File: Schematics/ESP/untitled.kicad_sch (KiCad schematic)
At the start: 10 parts, among them J10 Conn_01x03_Socket, J11 Conn_01x02_Pin, J12 Conn_01x02_Pin, J14 Conn_02x19_Odd_Even, J16 Conn_02x19_Odd_Even, J2 Conn_01x06_Pin, J7 Conn_01x07_Pin, J9 Conn_01x03_Socket

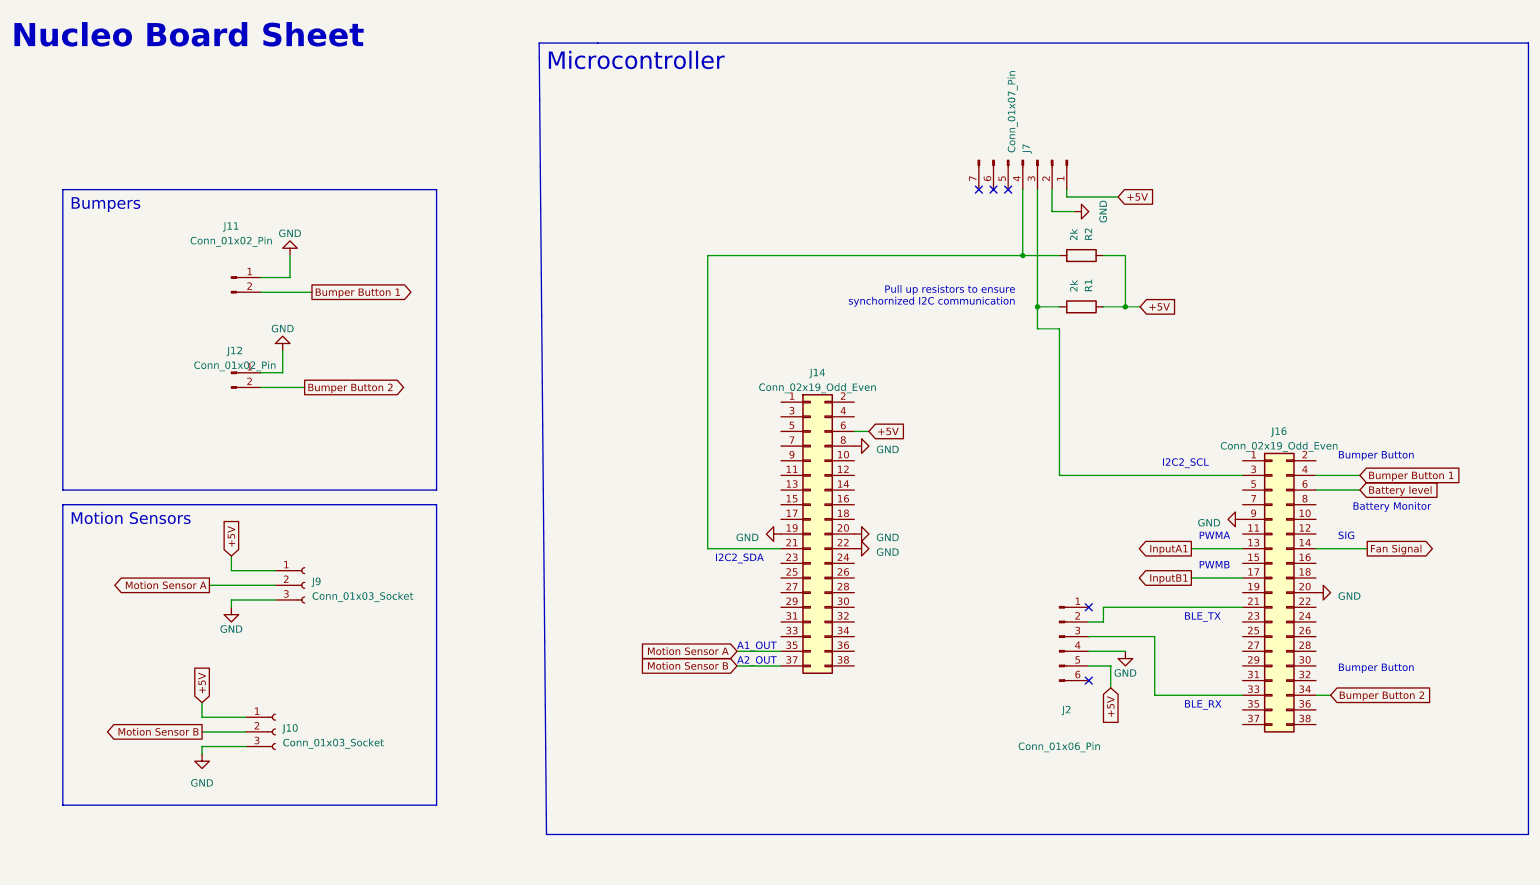
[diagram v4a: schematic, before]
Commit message: PCB layout done no wiring
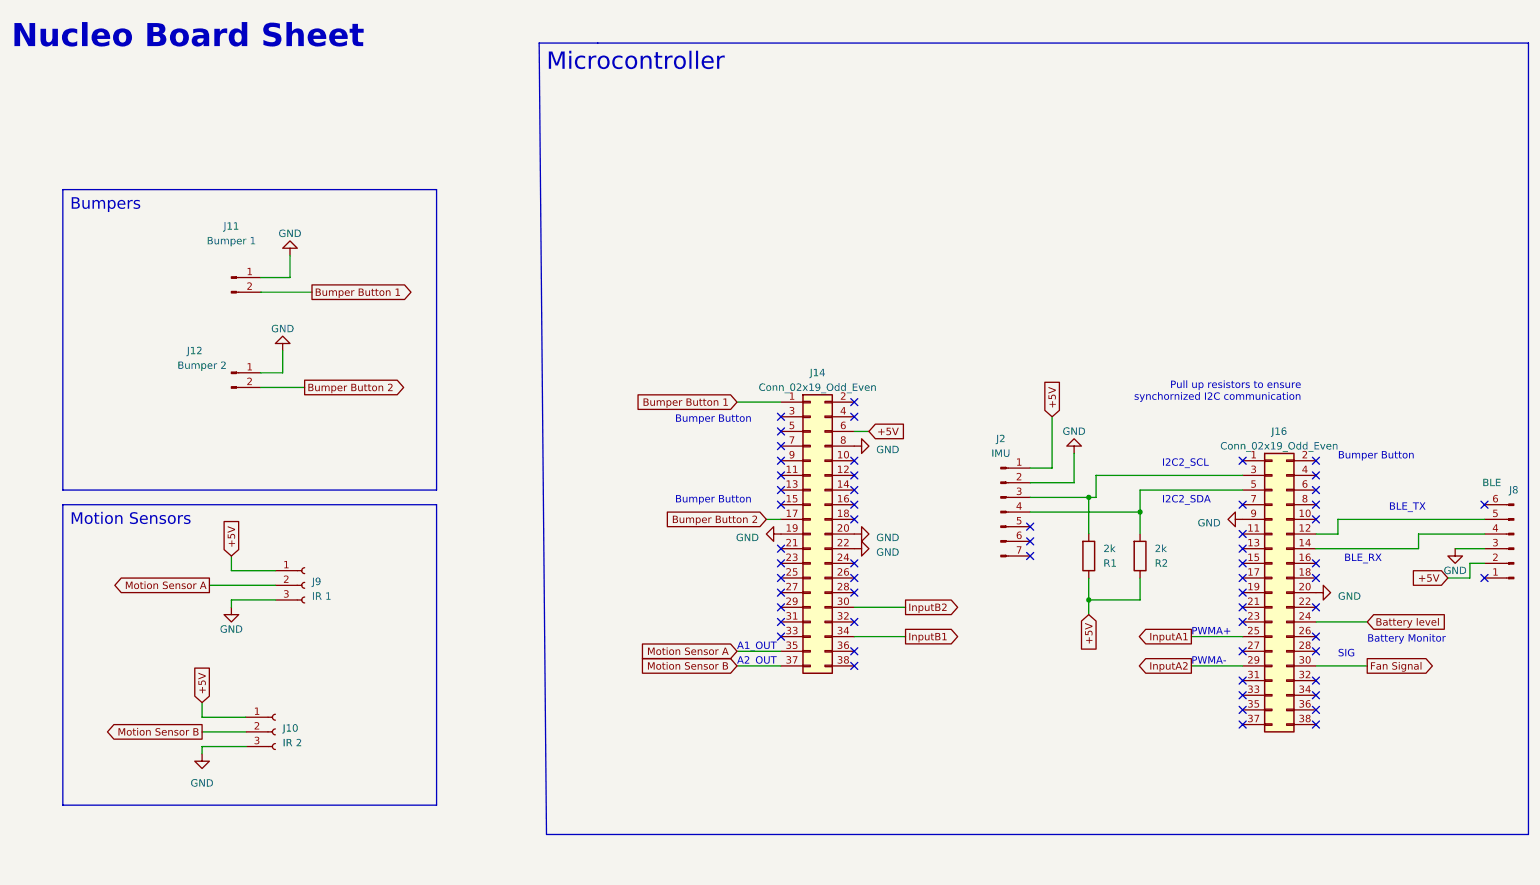
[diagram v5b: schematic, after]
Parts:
- removed J2: Conn_01x06_Pin, Connector_PinSocket_2.54mm:PinSocket_1x06_P2.54mm_Vertical, symbol Connector:Conn_01x06_Pin
- removed J7: Conn_01x07_Pin, Connector_PinSocket_2.54mm:PinSocket_1x07_P2.54mm_Vertical, symbol Connector:Conn_01x07_Pin
- added J2: IMU, Connector_PinSocket_2.54mm:PinSocket_1x07_P2.54mm_Vertical, symbol Connector:Conn_01x07_Pin
- added J8: BLE, Connector_PinSocket_2.54mm:PinSocket_1x06_P2.54mm_Vertical, symbol Connector:Conn_01x06_Pin
- J10: value Conn_01x03_Socket -> IR 2; footprint Connector_PinHeader_1.00mm:PinHeader_1x03_P1.00mm_Vertical -> Connector_PinHeader_2.54mm:PinHeader_1x03_P2.54mm_Vertical
- J11: value Conn_01x02_Pin -> Bumper 1; footprint Connector_PinSocket_1.00mm:PinSocket_1x02_P1.00mm_Vertical -> Connector_PinSocket_2.54mm:PinSocket_1x02_P2.54mm_Vertical
- J12: value Conn_01x02_Pin -> Bumper 2; footprint Connector_PinSocket_1.00mm:PinSocket_1x02_P1.00mm_Vertical -> Connector_PinSocket_2.54mm:PinSocket_1x02_P2.54mm_Vertical
- J9: value Conn_01x03_Socket -> IR 1; footprint Connector_PinHeader_1.00mm:PinHeader_1x03_P1.00mm_Vertical -> Connector_PinHeader_2.54mm:PinHeader_1x03_P2.54mm_Vertical
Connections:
- net +5V: now also J2.1 (Pin_1), J8.2 (Pin_2)
- net Battery level: now also J16.24 (Pin_24); no longer J16.6 (Pin_6)
- net Bumper Button 1: now also J14.1 (Pin_1); no longer J16.4 (Pin_4)
- net Bumper Button 2: now also J14.17 (Pin_17); no longer J16.34 (Pin_34)
- net Fan Signal: now also J16.30 (Pin_30); no longer J16.14 (Pin_14)
- net GND: now also J2.2 (Pin_2), J8.3 (Pin_3)
- net InputA1: now also J16.25 (Pin_25); no longer J16.13 (Pin_13)
- net InputB1: now also J14.34 (Pin_34); no longer J16.17 (Pin_17)
- net at J16.3 (Pin_3), R1.2: now also J2.3 (Pin_3)
- net at R2.2: now also J16.5 (Pin_5), J2.4 (Pin_4); no longer J14.21 (Pin_21)
- net InputB2: now reaches J14.30 (Pin_30)
- net at J16.12 (Pin_12): now also J8.5 (Pin_5)
- net InputA2: now reaches J16.29 (Pin_29)
- new net: J16.14 (Pin_14), J8.4 (Pin_4)
- no-connect marks 5 -> 60
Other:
- note added: "PWMA+"
- note added: "PWMA-"
- note removed: "PWMA"
- note removed: "PWMB"

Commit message: PCB layout done no wiring
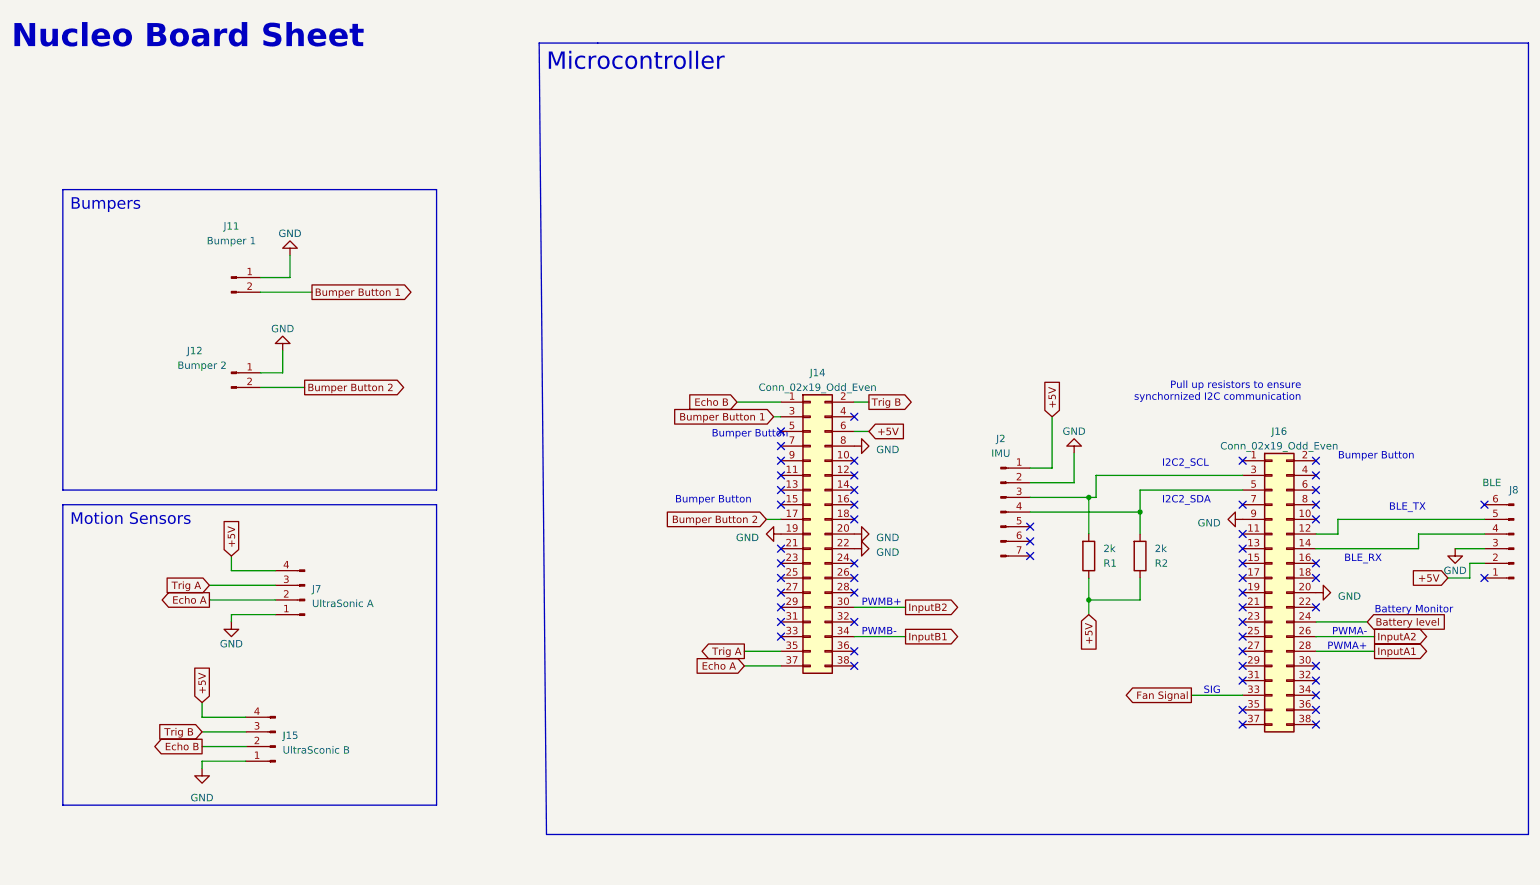
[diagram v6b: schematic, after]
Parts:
- removed J10: IR 2, Connector_PinHeader_2.54mm:PinHeader_1x03_P2.54mm_Vertical, symbol Connector:Conn_01x03_Socket
- removed J9: IR 1, Connector_PinHeader_2.54mm:PinHeader_1x03_P2.54mm_Vertical, symbol Connector:Conn_01x03_Socket
- added J15: UltraSconic B, Connector_PinHeader_2.54mm:PinHeader_1x04_P2.54mm_Vertical, symbol Connector:Conn_01x04_Pin
- added J7: UltraSonic A, Connector_PinHeader_2.54mm:PinHeader_1x04_P2.54mm_Vertical, symbol Connector:Conn_01x04_Pin
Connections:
- net +5V: now also J15.4 (Pin_4), J7.4 (Pin_4)
- net Bumper Button 1: now also J14.3 (Pin_3); no longer J14.1 (Pin_1)
- net Fan Signal: now also J16.33 (Pin_33); no longer J16.30 (Pin_30)
- net GND: now also J15.1 (Pin_1), J7.1 (Pin_1)
- net InputA1: now also J16.28 (Pin_28); no longer J16.25 (Pin_25)
- net InputA2: now also J16.26 (Pin_26); no longer J16.29 (Pin_29)
- net Trig B: now reaches J14.2 (Pin_2)
- net Trig B: now also J15.3 (Pin_3)
- net Motion Sensor A renamed Trig A
- net Trig A: now also J7.3 (Pin_3)
- net Motion Sensor B renamed Echo A
- net Echo A: now also J7.2 (Pin_2)
- new net Echo B: J14.1 (Pin_1), J15.2 (Pin_2)
- no-connect marks 60 -> 58
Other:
- note added: "PWMB+"
- note added: "PWMB-"
- note removed: "A1_OUT"
- note removed: "A2_OUT"
